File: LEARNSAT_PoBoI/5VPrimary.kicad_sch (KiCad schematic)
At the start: 17 parts, among them Q7 SI7164DP-T1-GE3, Q9 SI5418DU-T1-GE3, U20 INA219AIDCNR, U25 LTC4231IUD-2#TRPBF

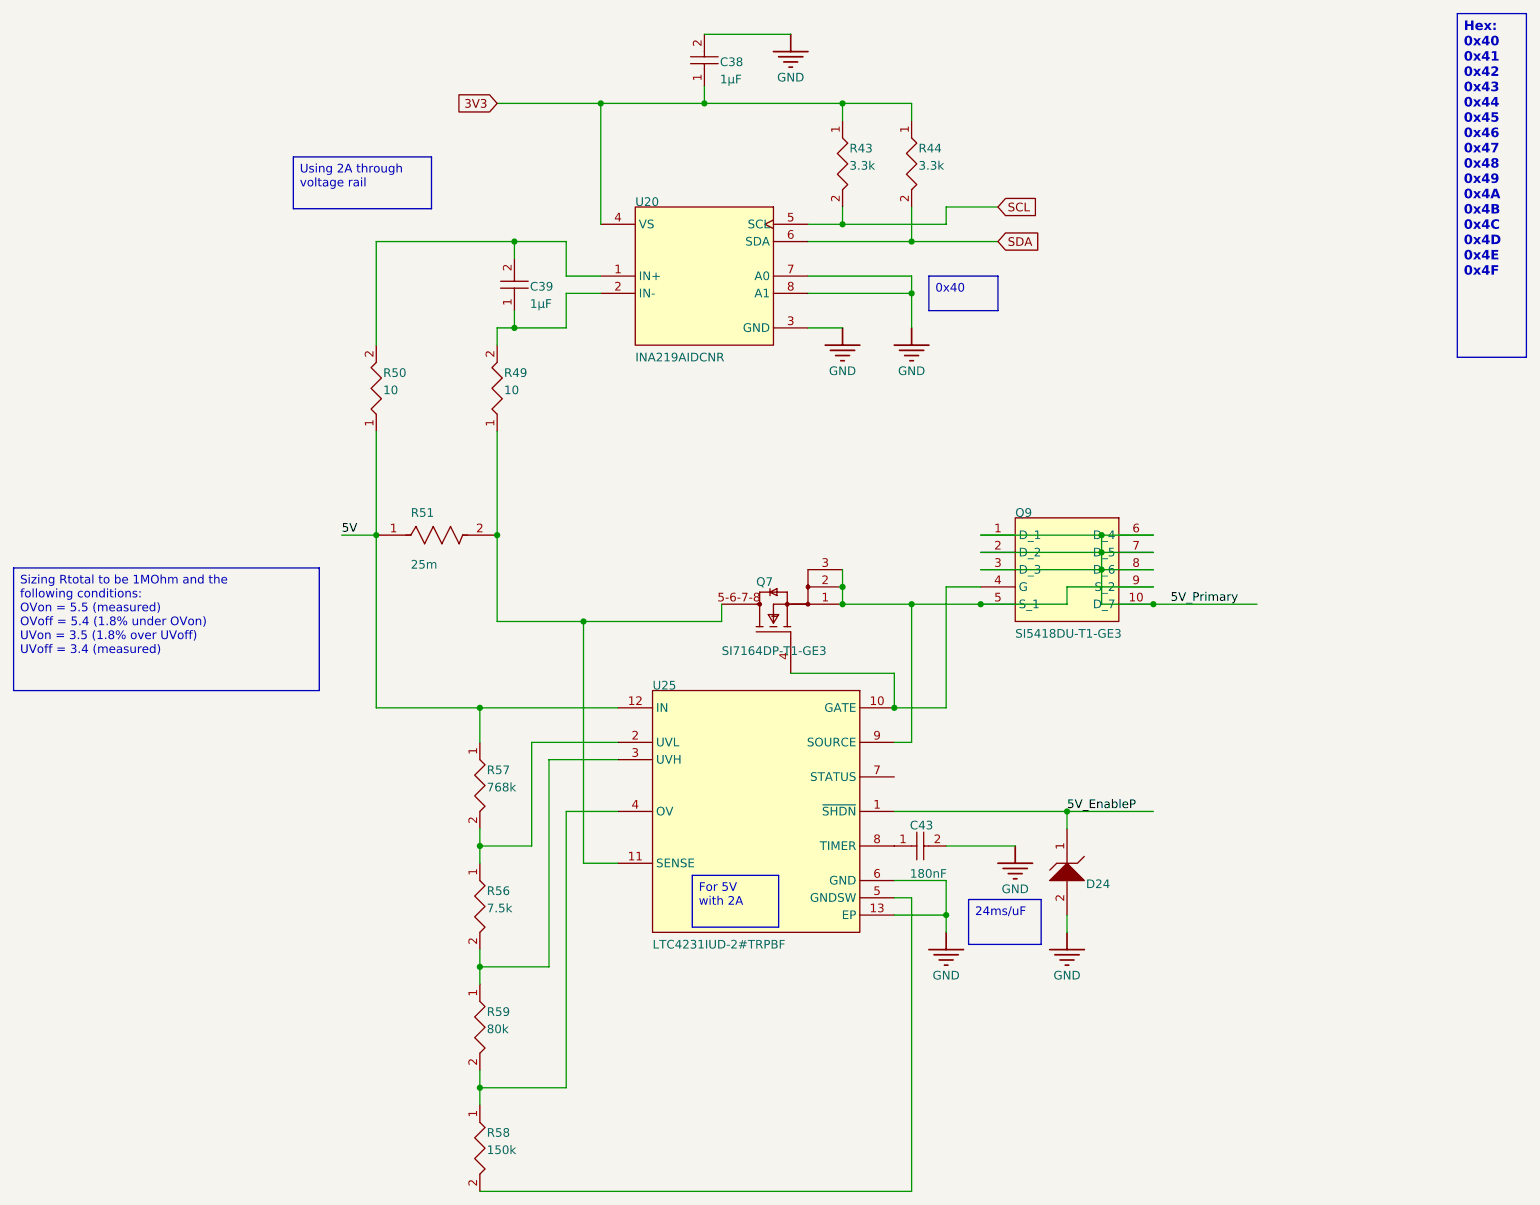
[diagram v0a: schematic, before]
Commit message: Added footprints
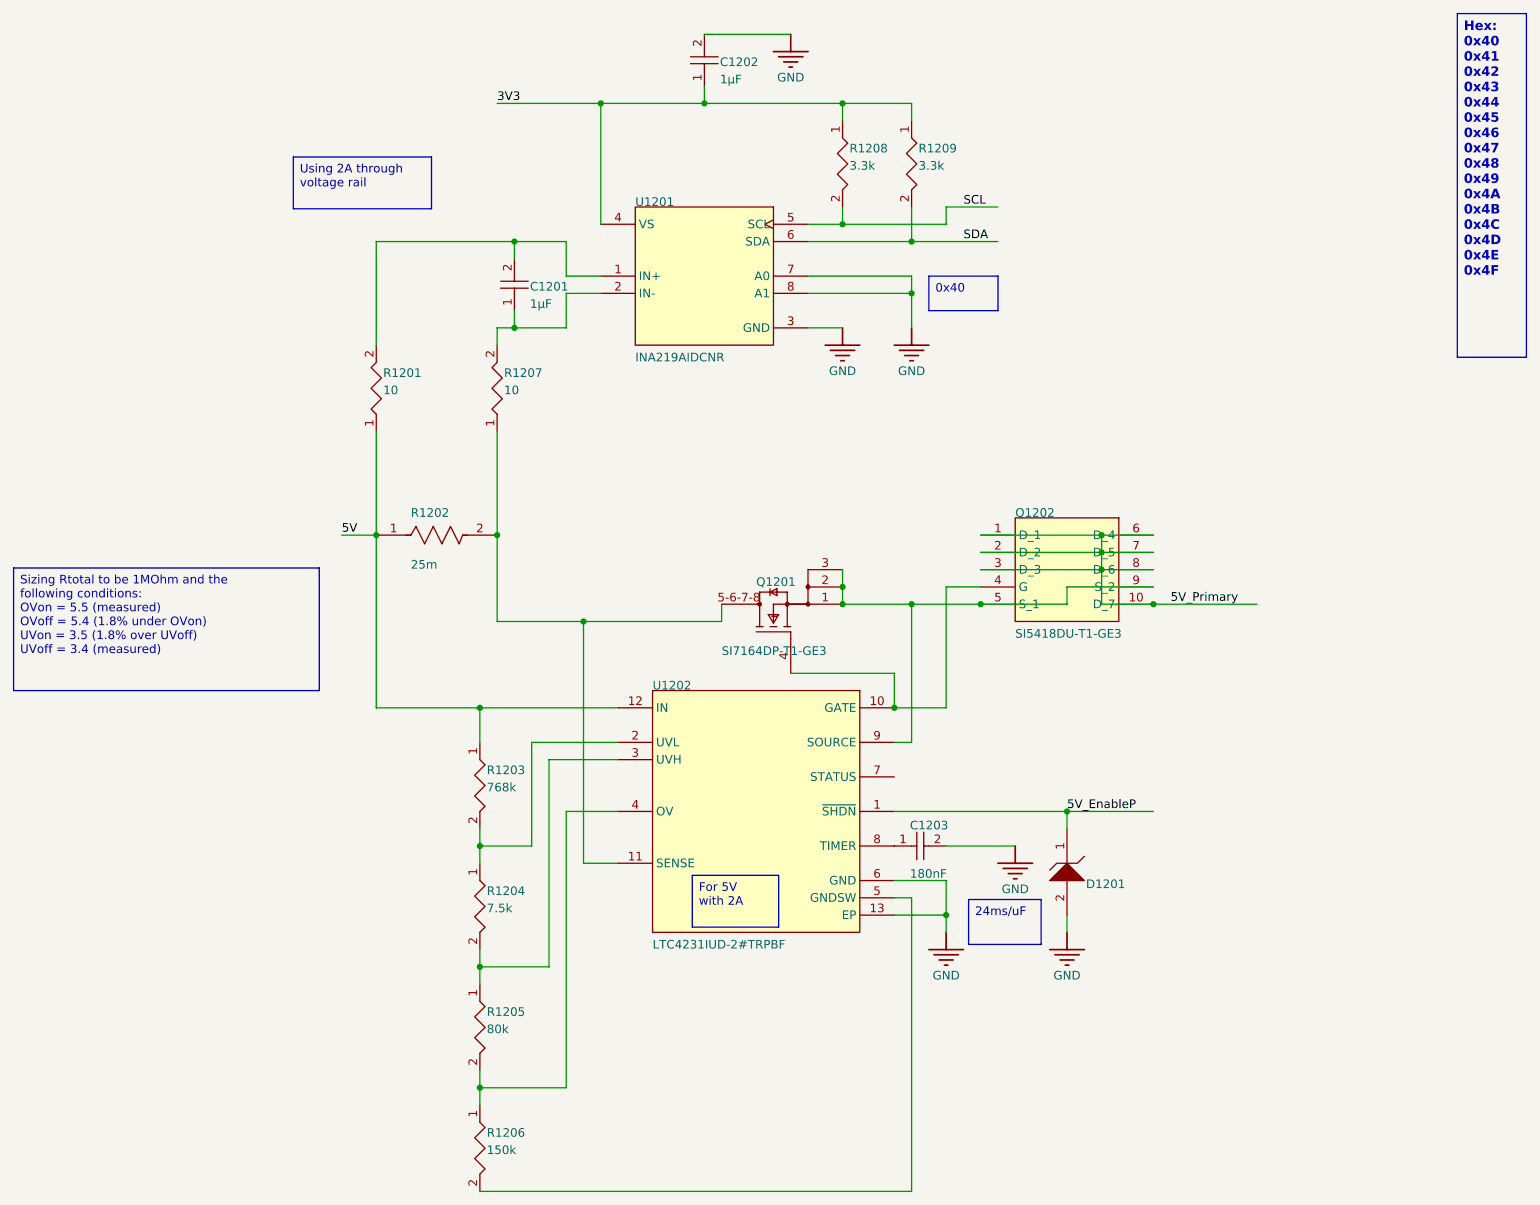
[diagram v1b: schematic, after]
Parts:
- C1201: renamed from C39; footprint CAPC1608X90X40LL10T20 -> Capacitor_SMD:C_0603_1608Metric
- C1202: renamed from C38; footprint CAPC1608X90X35ML15T15 -> Capacitor_SMD:C_0603_1608Metric
- C1203: renamed from C43; footprint FP-C0805C-DN-IPC_A -> Capacitor_SMD:C_0805_2012Metric
- D1201: renamed from D24; footprint ONSC-SOD-323-2-477-02_V -> Diode_SMD:D_SOD-323
- Q1201: renamed from Q7; footprint Vishay_S17-0173-SINGLE_MFG -> Package_SO:Vishay_PowerPAK_1212-8_Single
- Q1202: renamed from Q9; footprint SI5418DU-T1-GE3-Footprint-1 -> Package_SO:Vishay_PowerPAK_1212-8_Single
- R1201: renamed from R50; footprint RESC0402(1005)_L -> Resistor_SMD:R_0402_1005Metric
- R1202: renamed from R51; footprint FP-CSR1206-IPC_C -> Resistor_SMD:R_1206_3216Metric
- R1203: renamed from R57; footprint RESC0402(1005)_L -> Resistor_SMD:R_0402_1005Metric
- R1204: renamed from R56; footprint FP-CRCW1206-e3-IPC_A -> Resistor_SMD:R_1206_3216Metric
- R1205: renamed from R59; footprint FP-PTN0603-IPC_B -> Resistor_SMD:R_0603_1608Metric
- R1206: renamed from R58; footprint FP-RT1206-IPC_C -> Resistor_SMD:R_1206_3216Metric
- R1207: renamed from R49; footprint RESC0402(1005)_L -> Resistor_SMD:R_0402_1005Metric
- R1208: renamed from R43; footprint FP-CRCW1210-e3-IPC_C -> Resistor_SMD:R_1210_3225Metric
- R1209: renamed from R44; footprint FP-CRCW1210-e3-IPC_C -> Resistor_SMD:R_1210_3225Metric
- U1201: renamed from U20; footprint FP-DCN0008A-IPC_A -> INA219AIDCNR:SOT65P280X145-8N
- U1202: renamed from U25; footprint FP-UD-12-05-08-1855-IPC_A -> LTC4231IUD-2_TRPBF:QFN50P300X300X80-13N
